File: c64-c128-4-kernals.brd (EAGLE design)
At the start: 21.3 x 40.6 mm, 16 parts, among them IC1 27C512, IC2 PIC12F629P

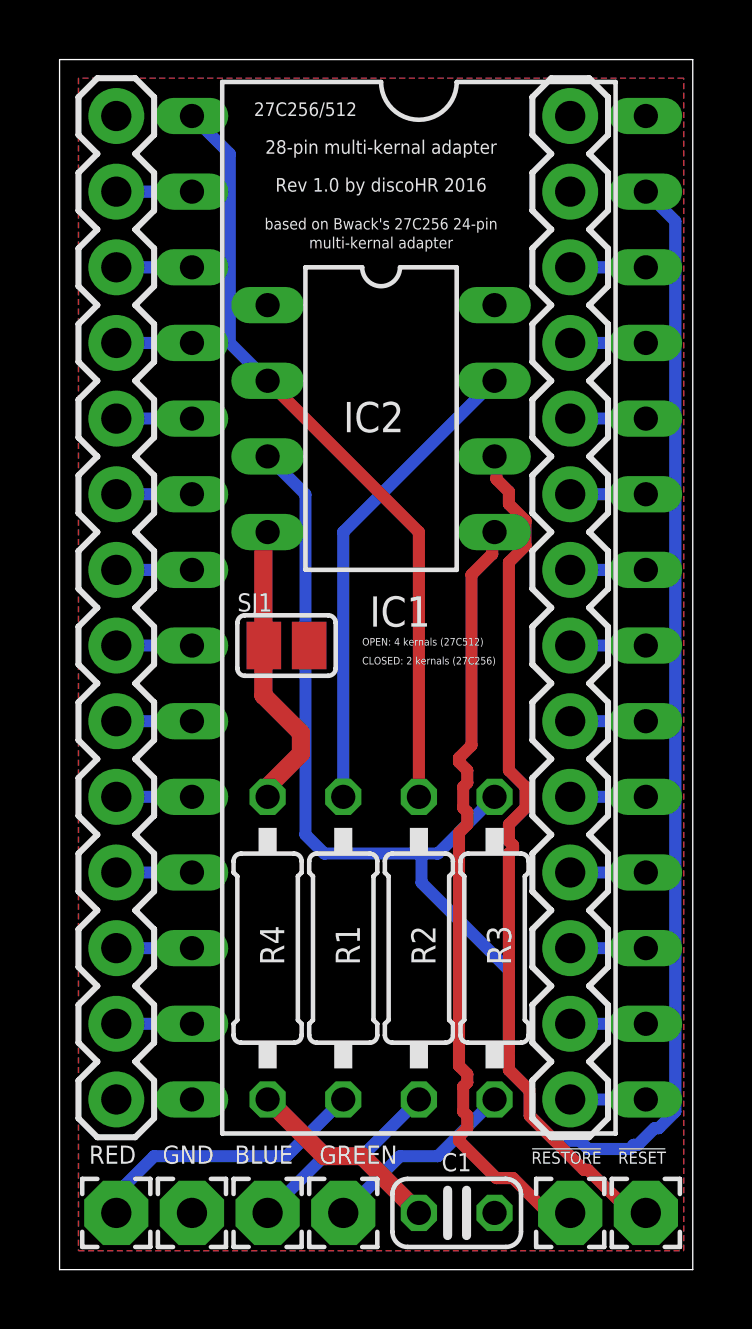
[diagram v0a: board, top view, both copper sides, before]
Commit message: removed R4 rearranged signal-pin pairs to allow using weak pull-up for the solder jumper minor design changes improved routing
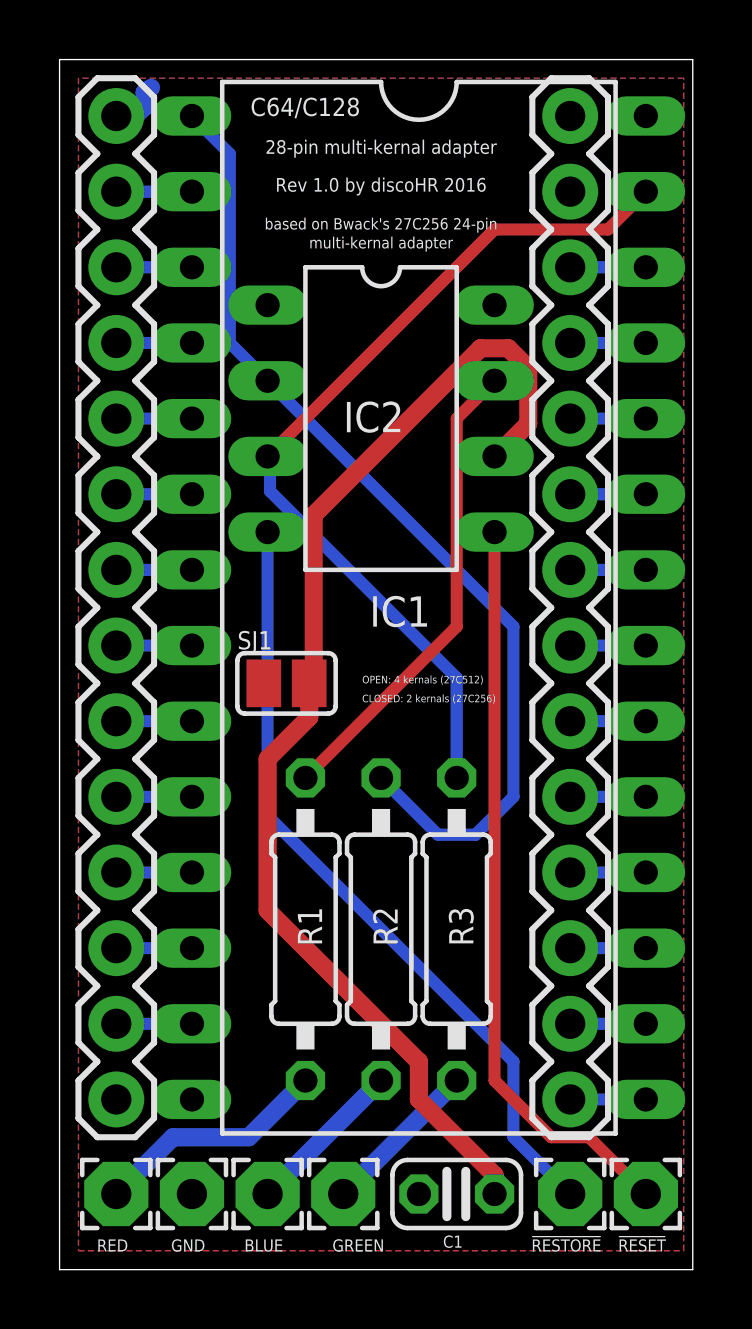
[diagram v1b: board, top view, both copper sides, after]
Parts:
- removed R4: 10k, resistor:0207/10
- moved R1 1.42 mm to (8.26, 11.4)
- moved R2 1.42 mm to (10.8, 11.4)
- moved R3 1.42 mm to (13.3, 11.4)
- moved SJ1 1.27 mm to (7.62, 19.7)
- moved !RESET! 0.64 mm to (19.7, 2.54)
- moved !RESTORE! 0.64 mm to (17.1, 2.54)
- moved BLUE 0.64 mm to (6.99, 2.54)
- moved C1 0.64 mm to (13.3, 2.54), turned to 180 degrees
- moved GND 0.64 mm to (4.45, 2.54)
- moved GREEN 0.64 mm to (9.53, 2.54)
- moved RED 0.64 mm to (1.91, 2.54)
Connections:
- removed net N$16: !RESTORE!.1, IC2.5
- net GND: now also SJ1.1; no longer SJ1.2
- net N$28: now also IC2.5; no longer IC2.6
- net N$31: now also !RESTORE!.1; no longer R4.2, SJ1.1
- net VCC: now also IC2.6, SJ1.2; no longer R4.1
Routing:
- net A14: track 68.2 -> 29.8 mm
- net VCC: track 6.66 -> 41.7 mm
- net N$16: track 26.4 -> 0.00 mm
- net N$31: track 9.94 -> 26.4 mm
- net A15: track 26.0 -> 33.1 mm
- net N$28: track 28.9 -> 25.1 mm
- net N$2: track 9.57 -> 7.93 mm
- net N$30: track 6.66 -> 5.39 mm
- net N$29: track 6.66 -> 5.39 mm
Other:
- board text added: "C64/C128"
- board text removed: "27C256/512"

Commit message: fixed incorrectly connected switch
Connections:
- new net N$16: IC2.6, SJ1.2
- net VCC: no longer IC2.6, SJ1.2
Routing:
- net VCC: track 41.7 -> 9.57 mm
- net N$16: track 0.00 -> 18.7 mm
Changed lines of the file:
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@@
 <vertex x="0.635" y="40.005"/>
 </polygon>
-<wire x1="2.54" y1="38.735" x2="1.905" y2="38.735" width="0.6096" layer="16"/>
-<wire x1="2.8575" y1="39.0525" x2="2.54" y2="38.735" width="0.6096" layer="16"/>
-<wire x1="2.8575" y1="39.52875" x2="2.8575" y2="39.0525" width="0.6096" layer="16"/>
-<wire x1="2.8575" y1="39.52875" x2="3.069021875" y2="39.682428125" width="0.6096" layer="16"/>
-<contactref element="SJ1" pad="2"/>
-<contactref element="IC2" pad="6"/>
-<wire x1="8.5344" y1="25.3365" x2="8.5344" y2="19.86915" width="0.6096" layer="1"/>
-<wire x1="14.1351" y1="30.9372" x2="8.5344" y2="25.3365" width="0.6096" layer="1"/>
-<wire x1="15.06855" y1="30.9372" x2="14.1351" y2="30.9372" width="0.6096" layer="1"/>
-<wire x1="15.7353" y1="30.27045" x2="15.06855" y2="30.9372" width="0.6096" layer="1"/>
-<wire x1="15.7353" y1="28.40355" x2="15.7353" y2="30.27045" width="0.6096" layer="1"/>
-<wire x1="14.6685" y1="27.33675" x2="15.7353" y2="28.40355" width="0.6096" layer="1"/>
-<wire x1="8.5344" y1="19.86915" x2="8.382" y2="19.685" width="0.6096" layer="1"/>
-<wire x1="14.6685" y1="27.33675" x2="14.605" y2="27.305" width="0.6096" layer="1"/>
-<wire x1="14.605" y1="2.54" x2="14.605" y2="3.175" width="0.6096" layer="1"/>
-<wire x1="14.605" y1="3.175" x2="12.065" y2="5.715" width="0.6096" layer="1"/>
-<wire x1="12.065" y1="5.715" x2="12.065" y2="6.985" width="0.6096" layer="1"/>
-<wire x1="12.065" y1="6.985" x2="6.985" y2="12.065" width="0.6096" layer="1"/>
-<wire x1="6.985" y1="12.065" x2="6.985" y2="17.145" width="0.6096" layer="1"/>
-<wire x1="8.382" y1="19.685" x2="8.382" y2="18.542" width="0.6096" layer="1"/>
-<wire x1="8.382" y1="18.542" x2="6.985" y2="17.145" width="0.6096" layer="1"/>
+<wire x1="6.985" y1="32.385" x2="6.985" y2="35.56" width="0.6096" layer="16"/>
+<wire x1="6.985" y1="35.56" x2="5.08" y2="37.465" width="0.6096" layer="16"/>
+<wire x1="5.08" y1="37.465" x2="3.175" y2="37.465" width="0.6096" layer="16"/>
+<wire x1="3.175" y1="37.465" x2="1.905" y2="38.735" width="0.6096" layer="16"/>
 </signal>
 <signal name="GND" class="1">
@@
 <contactref element="IC2" pad="2"/>
 <contactref element="R2" pad="2"/>
-<wire x1="6.985" y1="29.845" x2="5.715" y2="31.115" width="0.4064" layer="16"/>
-<wire x1="5.715" y1="31.115" x2="5.715" y2="37.465" width="0.4064" layer="16"/>
-<wire x1="5.715" y1="37.465" x2="4.445" y2="38.735" width="0.4064" layer="16"/>
 <wire x1="10.795" y1="16.51" x2="12.7" y2="14.605" width="0.4064" layer="16"/>
 <wire x1="12.7" y1="14.605" x2="13.97" y2="14.605" width="0.4064" layer="16"/>
@@
 <wire x1="15.24" y1="15.875" x2="15.24" y2="21.59" width="0.4064" layer="16"/>
 <wire x1="15.24" y1="21.59" x2="6.985" y2="29.845" width="0.4064" layer="16"/>
+<wire x1="6.985" y1="29.845" x2="5.715" y2="31.115" width="0.4064" layer="1"/>
+<wire x1="5.715" y1="31.115" x2="5.715" y2="37.465" width="0.4064" layer="1"/>
+<wire x1="5.715" y1="37.465" x2="4.445" y2="38.735" width="0.4064" layer="1"/>
 </signal>
 <signal name="A14">
@@
 <wire x1="6.985" y1="15.24" x2="6.985" y2="24.765" width="0.4064" layer="16"/>
 </signal>
+<signal name="N$16">
+<contactref element="IC2" pad="6"/>
+<contactref element="SJ1" pad="2"/>
+<wire x1="8.40105" y1="25.0698" x2="8.40105" y2="19.7358" width="0.4064" layer="1"/>
+<wire x1="14.26845" y1="30.9372" x2="8.40105" y2="25.0698" width="0.4064" layer="1"/>
+<wire x1="14.9352" y1="30.9372" x2="14.26845" y2="30.9372" width="0.4064" layer="1"/>
+<wire x1="15.60195" y1="30.27045" x2="14.9352" y2="30.9372" width="0.4064" layer="1"/>
+<wire x1="15.60195" y1="28.2702" x2="15.60195" y2="30.27045" width="0.4064" layer="1"/>
+<wire x1="14.6685" y1="27.33675" x2="15.60195" y2="28.2702" width="0.4064" layer="1"/>
+<wire x1="8.40105" y1="19.7358" x2="8.382" y2="19.685" width="0.4064" layer="1"/>
+<wire x1="14.6685" y1="27.33675" x2="14.605" y2="27.305" width="0.4064" layer="1"/>
+</signal>
 </signals>
